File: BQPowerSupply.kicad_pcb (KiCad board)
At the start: 2 copper layers, 31.7 x 18.5 mm, 34 parts

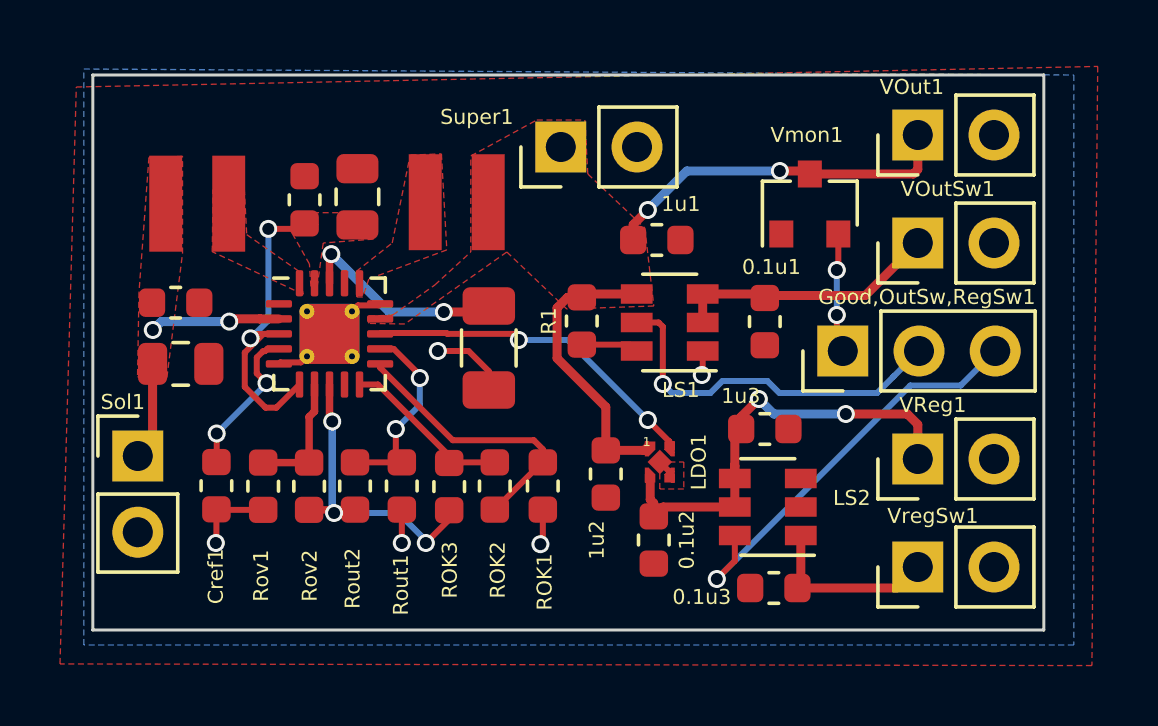
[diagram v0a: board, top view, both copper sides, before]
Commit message: Rev 2 without voltage monitor, with SOT23-5 for LDO
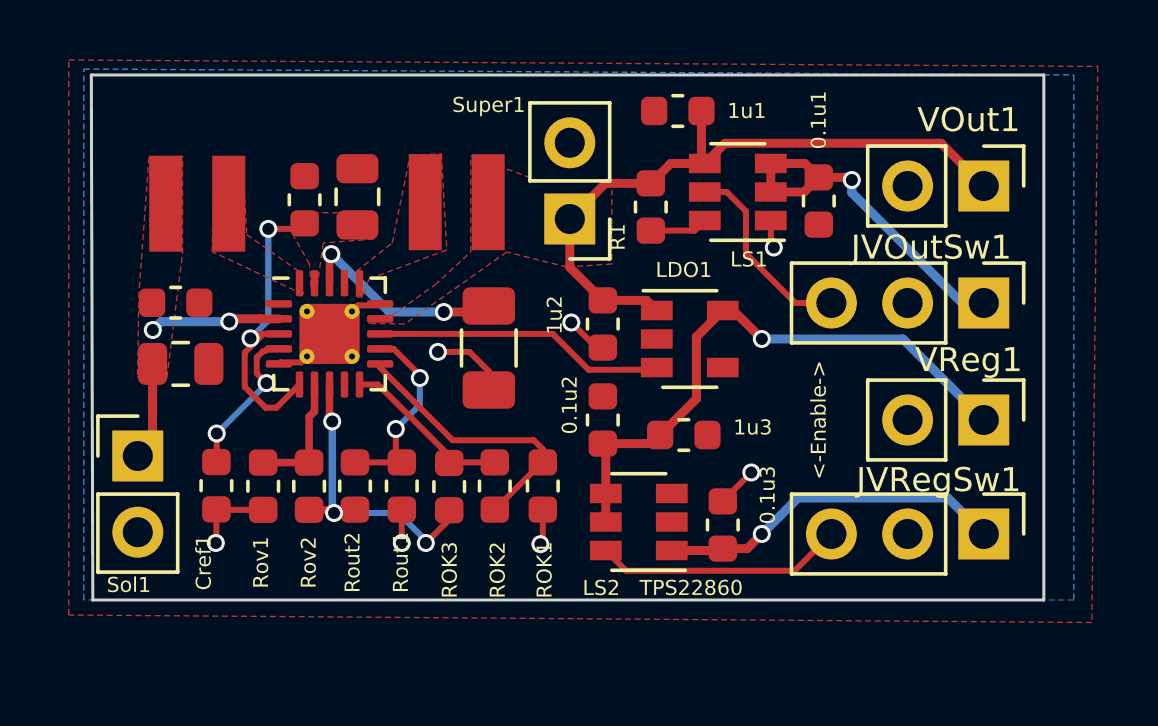
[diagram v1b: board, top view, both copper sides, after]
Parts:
- removed Good,OutSw,RegSw1: Conn_01x03, Connector_PinHeader_2.54mm:PinHeader_1x03_P2.54mm_Vertical
- removed VOutSw1, VregSw1: Conn_01x02, Connector_PinHeader_2.54mm:PinHeader_1x02_P2.54mm_Vertical
- removed Vmon1: TPS3839-3.1V, Package_TO_SOT_SMD:SOT-23
- added JVOutSw1: Conn_01x03, Connector_PinHeader_2.54mm:PinHeader_1x03_P2.54mm_Vertical, F.Cu at (187.0, 79.6)
- added JVRegSw1: Conn_01x03, Connector_PinHeader_2.54mm:PinHeader_1x03_P2.54mm_Vertical, F.Cu at (187.0, 87.3)
- LDO1: value TPS7A02-4X2SON -> TPS7A02_3.6; footprint myFootprints:DQN_X2SON -> Package_TO_SOT_SMD:SOT-23-5
- ROK2: value 5.36M -> 4,42M
- ROK3: value 1M -> 0.510M
- moved 1u2 5.00 mm to (174.3, 80.3)
- moved LS1 4.91 mm to (178.8, 75.9)
- moved R1 4.44 mm to (175.9, 76.4)
- moved 0.1u1 4.40 mm to (181.5, 76.2)
- moved 1u1 4.36 mm to (176.8, 73.2), turned to 180 degrees
- moved 0.1u2 4.35 mm to (174.3, 83.5), turned to 90 degrees
- moved LS2 4.33 mm to (175.5, 86.9)
- moved LDO1 4.22 mm to (177.2, 80.8), turned to 0 degrees
- moved VOut1 2.78 mm to (187.0, 75.7), turned to 270 degrees
- moved 1u3 2.71 mm to (177.0, 84.0)
- moved 0.1u3 2.70 mm to (178.3, 87.0), turned to 90 degrees
- moved VReg1 2.56 mm to (187.0, 83.5), turned to 270 degrees
- moved Super1 2.42 mm to (173.2, 76.8), turned to 180 degrees
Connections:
- LDO1 pad 1: Vreg -> VOut
- LDO1 pad 4: VOut -> (no net)
- LDO1 pad 5: GND -> Vreg
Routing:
- net VOutSwEn: track 12.4 -> 6.58 mm, vias 1 -> 0
- net VRegSwEn: track 14.1 -> 8.31 mm, vias 1 -> 0
- net VregSw: track 6.10 -> 11.6 mm, vias 0 -> 1
- net Vreg: track 15.9 -> 19.9 mm, vias 2 -> 1
- net VOutGood: track 4.00 -> 0.00 mm, vias 2 -> 0
- net VOutSw: track 8.93 -> 12.0 mm, vias 0 -> 1
- net GND: track 12.2 -> 14.4 mm, vias 5 -> 7
- net VBatOK: track 11.5 -> 9.75 mm, vias 2 -> 0
- net VOut: track 21.7 -> 22.3 mm, vias 2 -> 0
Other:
- board size 31.7 x 18.5 mm -> 31.8 x 17.5 mm
- board text added: "<-Enable->"
- board text added: "BQ25570PowerSupply Rev 2 L. Konneker"
- board text added: "TPS22860"
